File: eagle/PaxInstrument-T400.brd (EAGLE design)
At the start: 99.1 x 50.8 mm, 132 parts, among them IC1 MCP3424, IC3 SN74LVC1G74DCT, J1 MICRO-SDCARD-CONNECTOR-330006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, Q1 DMP2035U-7, Q2 DMP2035U-7, Q3 DMN2075U-7, Q4 DMN2075U-7, Q5 DMP2035U-7, U1 MCP9800, U2 APX809, U3 MCP73831, U4 MIC5219-3.3V, X1 FH12-12S-1S, Y1 RESONATORSMD

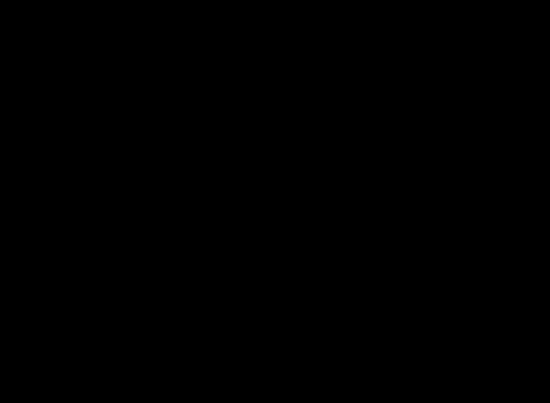
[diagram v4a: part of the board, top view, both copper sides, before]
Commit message: Updated battery detect circuit in Sch and PCB layout
- Internal analog reference voltage #156
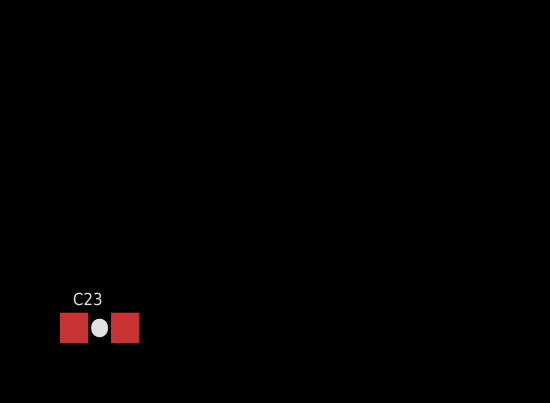
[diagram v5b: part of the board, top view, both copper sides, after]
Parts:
- added C23: 0.1uF, PaxInstrument-T400:SPARKFUN-CAPACITORS_0603-CAP
- R20: value 10k -> 18.7K
- R24: value 10K -> 34K
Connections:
- net GND: now also C23.2
- net VBAT_SENSE: now also C23.1
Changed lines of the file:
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@@
 <layer number="19" name="Unrouted" color="6" fill="1" visible="yes" active="yes"/>
 <layer number="20" name="Dimension" color="13" fill="1" visible="yes" active="yes"/>
-<layer number="21" name="tPlace" color="7" fill="1" visible="yes" active="yes"/>
-<layer number="22" name="bPlace" color="14" fill="1" visible="no" active="yes"/>
+<layer number="21" name="tPlace" color="7" fill="1" visible="no" active="yes"/>
+<layer number="22" name="bPlace" color="14" fill="1" visible="yes" active="yes"/>
 <layer number="23" name="tOrigins" color="15" fill="1" visible="yes" active="yes"/>
 <layer number="24" name="bOrigins" color="15" fill="1" visible="no" active="yes"/>
@@
 <attribute name="MF" value="FCI" x="87.63" y="33.02" size="1.778" layer="28" rot="MR90" display="off"/>
 </element>
-<element name="R20" library="PaxInstrument-T400" package="SPARKFUN-RESISTORS_0603-RES" value="10k" x="84.93125" y="17.62125" smashed="yes" rot="R270">
+<element name="R20" library="PaxInstrument-T400" package="SPARKFUN-RESISTORS_0603-RES" value="18.7K" x="84.93125" y="17.62125" smashed="yes" rot="R270">
 <attribute name="MPN" value="" x="84.93125" y="17.62125" size="1.778" layer="27" rot="R270" display="off"/>
 <attribute name="NAME" x="84.8995" y="16.8275" size="0.4064" layer="25" rot="R90" align="center"/>
@@
 <attribute name="MF" value="DIODES INC" x="12.620625" y="1.27" size="1.778" layer="27" rot="R180" display="off"/>
 </element>
-<element name="R24" library="PaxInstrument-T400" package="SPARKFUN-RESISTORS_0603-RES" value="10K" x="86.51875" y="17.62125" smashed="yes" rot="R270">
+<element name="R24" library="PaxInstrument-T400" package="SPARKFUN-RESISTORS_0603-RES" value="34K" x="86.51875" y="17.62125" smashed="yes" rot="R270">
 <attribute name="MPN" value="" x="86.51875" y="17.62125" size="1.778" layer="27" rot="R270" display="off"/>
 <attribute name="NAME" x="86.45525" y="16.764" size="0.4064" layer="25" rot="R270" align="center"/>
@@
 <element name="R23" library="PaxInstrument-T400" package="SPARKFUN-RESISTORS_0603-RES" value="10k" x="79.375" y="22.70125" rot="R270">
 <attribute name="MPN" value="" x="79.375" y="22.70125" size="1.778" layer="27" rot="R270" display="off"/>
+</element>
+<element name="C23" library="PaxInstrument-T400" package="SPARKFUN-CAPACITORS_0603-CAP" value="0.1uF" x="-42.545" y="-39.37">
+<attribute name="MPN" value="" x="-42.545" y="-39.37" size="1.778" layer="27" display="off"/>
 </element>
 </elements>
@@
 <via x="95.09125" y="21.87575" extent="1-16" drill="0.3302"/>
 <via x="88.265" y="26.035" extent="1-16" drill="0.3302"/>
+<contactref element="C23" pad="2"/>
+<wire x1="4.064" y1="10.922" x2="-41.695" y2="-39.37" width="0" layer="19" extent="1-1"/>
 </signal>
 <signal name="D-">
@@
 <wire x1="28.773990625" y1="23.97125" x2="27.9254625" y2="23.97125" width="0.3048" layer="1"/>
 <wire x1="27.24126875" y1="23.28705625" x2="27.9254625" y2="23.97125" width="0.3048" layer="1"/>
+<contactref element="C23" pad="1"/>
+<wire x1="27.24126875" y1="23.28705625" x2="-43.395" y2="-39.37" width="0" layer="19" extent="1-1"/>
 </signal>
 <signal name="RTC_INT">

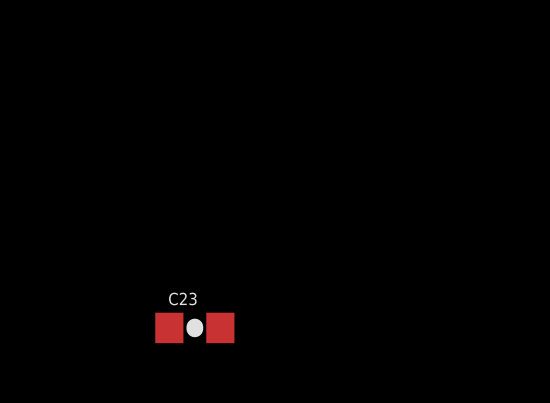
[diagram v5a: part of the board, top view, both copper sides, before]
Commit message: updated schematic
- Add 4.7k pulldown to VBUS input #188
- Internal analog reference voltage #156
- DPN pull-up resisors #191
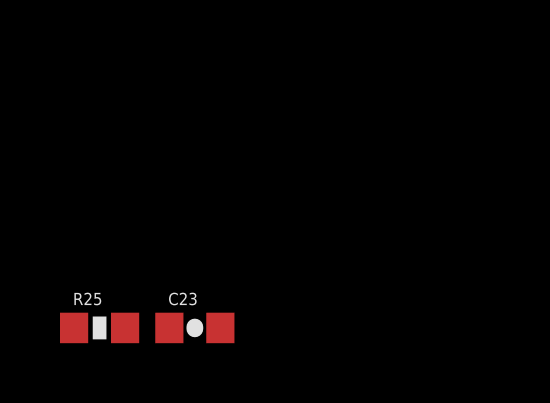
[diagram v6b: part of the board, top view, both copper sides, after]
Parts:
- added R25: 10k, PaxInstrument-T400:SPARKFUN-RESISTORS_0603-RES
- C23: value 0.1uF -> 1uF
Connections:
- net GND: now also R25.1
- net VBUS_IN: now also R25.2

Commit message: Updated SCH and PCB
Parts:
- JP1: value (none) -> ON
- moved C23 144.1 mm to (88.8, 20.0)
- moved R25 69.9 mm to (9.21, 3.81), turned to 270 degrees
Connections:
- removed net DATA1: GND.37, ICSP1.4, U$3.37
- new net RXLED: GND.8, U$3.8
- net PWR_ONOFF: now also GND.37, U$3.37; no longer GND.12, U$3.12
- net RTC_INT: now also GND.28, U$3.28; no longer GND.1, U$3.1
- net SW_C: now also GND.12, U$3.12; no longer GND.28, U$3.28
- net SW_PWR: now also GND.1, U$3.1; no longer GND.8, U$3.8
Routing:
- net DATA1: track 99.0 -> 0.00 mm, vias 3 -> 0
- net SW_PWR: track 22.3 -> 6.02 mm
- net PWR_ONOFF: track 15.3 -> 4.18 mm
- net SW_C: track 84.5 -> 79.1 mm
- net RTC_INT: track 70.4 -> 66.5 mm
- net TXLED: track 3.02 -> 0.00 mm
- net VBAT_SENSE: track 65.7 -> 68.5 mm
- net VBUS_IN: track 142.5 -> 144.2 mm
- net GND: vias 107 -> 105

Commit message: Updated PCB layout
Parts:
- moved TP1 22.2 mm to (34.6, 23.2)
- moved Q4 21.0 mm to (36.2, 21.6), turned to 0 degrees
- moved R22 16.2 mm to (33.0, 21.6)
- moved R18 6.50 mm to (17.9, 9.97), turned to 90 degrees
- moved C19 3.81 mm to (33.0, 25.4), turned to 90 degrees
- moved Q5 2.54 mm to (14.8, 9.97)
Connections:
- removed net TXLED: GND.22, U$3.22
- new net DATA1: GND.37, ICSP1.4, U$3.37
- net PWR_ONOFF: now also GND.22, U$3.22; no longer GND.37, U$3.37
- net RTC_INT: now also GND.20, U$3.20; no longer GND.28, U$3.28
- net SW_A: now also GND.1, U$3.1; no longer GND.21, U$3.21
- net SW_B: now also GND.21, U$3.21; no longer GND.20, U$3.20
- net SW_C: now also GND.28, U$3.28; no longer GND.12, U$3.12
- net SW_PWR: now also GND.12, U$3.12; no longer GND.1, U$3.1
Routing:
- net DATA1: track 0.00 -> 95.9 mm, vias 0 -> 3
- net N$27: track 8.30 -> 86.0 mm, vias 0 -> 6
- net SW_A: track 82.3 -> 107.5 mm, vias 2 -> 4
- net RTC_INT: track 66.5 -> 45.1 mm, vias 4 -> 2
- net SW_PWR: track 6.02 -> 25.8 mm
- net PWR_ONOFF: track 4.18 -> 9.96 mm
- net SW_C: track 79.1 -> 84.5 mm
- net 3.3V: track 389.5 -> 385.4 mm, vias 22 -> 23
- net RXLED: track 0.00 -> 2.65 mm
- net DATA2: track 90.3 -> 88.5 mm
- net LCD_BL: track 58.8 -> 58.2 mm
- net GND: vias 105 -> 106
